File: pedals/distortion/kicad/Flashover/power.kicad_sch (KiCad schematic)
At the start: 13 parts, among them J3 9V DC, U2 TL072, U3 78L05

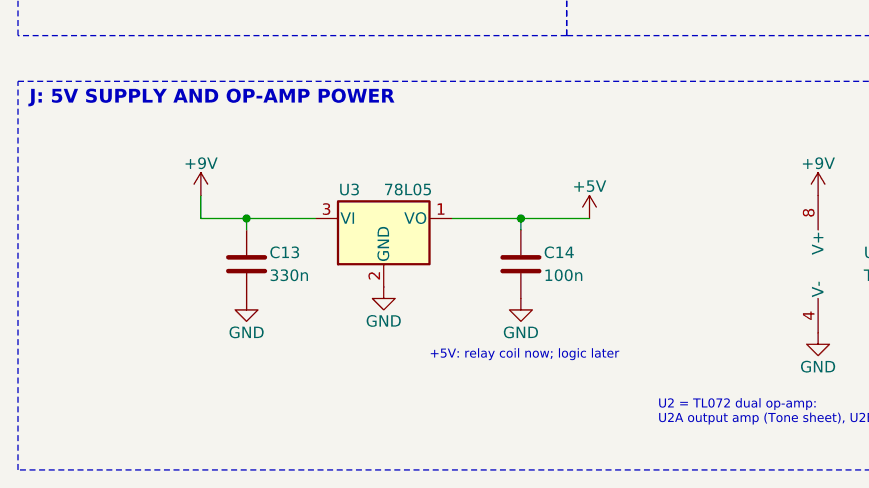
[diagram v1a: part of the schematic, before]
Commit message: Add Flashover controls and LED ring sheets
Controls sheet: three PEC11R encoders with push switches (pull-ups and
RC filtering) and the Soft/Hard button. LED Rings sheet: IS31FL3236A
driving three 11-LED rings plus Soft, Hard and On LEDs, on its own I2C
bus. Controller sheet wires the new GPIOs; the 5V regulator becomes an
L7805 for the LED load. ERC clean.

Co-Authored-By: Claude Opus 5.5 <noreply@anthropic.com>
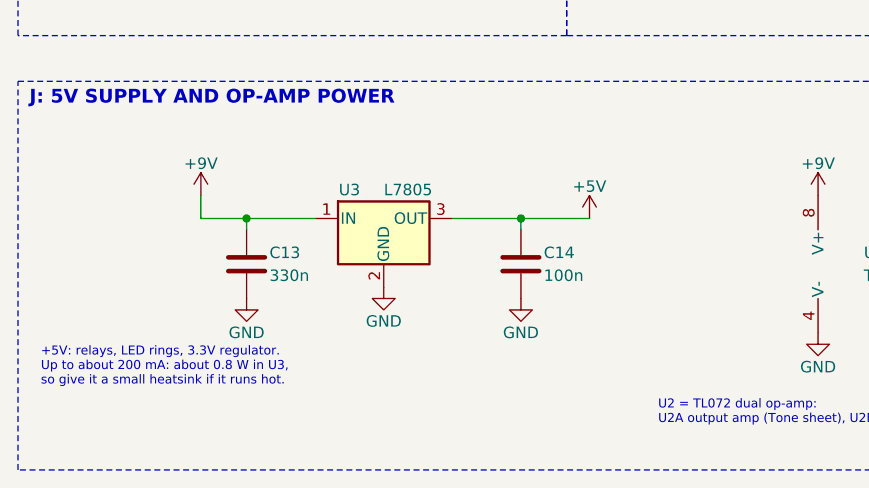
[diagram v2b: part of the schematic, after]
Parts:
- removed U3: 78L05, symbol Regulator_Linear:L78L05_TO92
- added U3: L7805, symbol Regulator_Linear:L7805
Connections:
- net +5V: now also U3.3 (OUT)
- net +9V: now also U3.1 (IN)
- net GND: now also U3.2 (GND)
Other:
- note added: "+5V: relays, LED rings, 3.3V regulator. Up to about 200 mA: about 0.8 W in U3, so give it a small heatsink if it runs hot."
- note removed: "+5V: relay coil now; logic later"
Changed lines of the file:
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@@
 	(title_block
 		(title "Flashover - Power and Bias")
-		(date "2026-10-08")
+		(date "2026-10-09")
 		(rev "0.1")
 		(company "GreywireStudio")
@@
 		(effects (font (size 1 1)) (justify left))
 	)
-	(text "+5V: relay coil now; logic later"
-		(exclude_from_sim no)
-		(at 66.04 139.7 0)
+	(text "+5V: relays, LED rings, 3.3V regulator.\nUp to about 200 mA: about 0.8 W in U3,\nso give it a small heatsink if it runs hot."
+		(exclude_from_sim no)
+		(at 22.86 140.97 0)
 		(effects (font (size 1 1)) (justify left))
 	)
@@
 		(instances
 			(project "Flashover"
-				(path "/37bda491-c0dc-4d48-acdf-49df4f139bb0/553416c4-a47b-4eba-a37d-be64f47f9e32"
+				(path "/ea9f0b88-0903-4174-9c8e-623c203001c6/73170522-0a6a-467c-b01f-a30637312dcb"
 					(reference "J3")
 					(unit 1)
@@
 		(instances
 			(project "Flashover"
-				(path "/37bda491-c0dc-4d48-acdf-49df4f139bb0/553416c4-a47b-4eba-a37d-be64f47f9e32"
+				(path "/ea9f0b88-0903-4174-9c8e-623c203001c6/73170522-0a6a-467c-b01f-a30637312dcb"
 					(reference "D3")
 					(unit 1)
@@
 		(instances
 			(project "Flashover"
-				(path "/37bda491-c0dc-4d48-acdf-49df4f139bb0/553416c4-a47b-4eba-a37d-be64f47f9e32"
+				(path "/ea9f0b88-0903-4174-9c8e-623c203001c6/73170522-0a6a-467c-b01f-a30637312dcb"
 					(reference "#PWR23")
 					(unit 1)
@@
 		(instances
 			(project "Flashover"
-				(path "/37bda491-c0dc-4d48-acdf-49df4f139bb0/553416c4-a47b-4eba-a37d-be64f47f9e32"
+				(path "/ea9f0b88-0903-4174-9c8e-623c203001c6/73170522-0a6a-467c-b01f-a30637312dcb"
 					(reference "#FLG01")
 					(unit 1)
@@
 		(instances
 			(project "Flashover"
-				(path "/37bda491-c0dc-4d48-acdf-49df4f139bb0/553416c4-a47b-4eba-a37d-be64f47f9e32"
+				(path "/ea9f0b88-0903-4174-9c8e-623c203001c6/73170522-0a6a-467c-b01f-a30637312dcb"
 					(reference "#PWR24")
 					(unit 1)
@@
 		(instances
 			(project "Flashover"
-				(path "/37bda491-c0dc-4d48-acdf-49df4f139bb0/553416c4-a47b-4eba-a37d-be64f47f9e32"
+				(path "/ea9f0b88-0903-4174-9c8e-623c203001c6/73170522-0a6a-467c-b01f-a30637312dcb"
 					(reference "C7")
 					(unit 1)
@@
 		(instances
 			(project "Flashover"
-				(path "/37bda491-c0dc-4d48-acdf-49df4f139bb0/553416c4-a47b-4eba-a37d-be64f47f9e32"
+				(path "/ea9f0b88-0903-4174-9c8e-623c203001c6/73170522-0a6a-467c-b01f-a30637312dcb"
 					(reference "#PWR25")
 					(unit 1)
@@
 		(instances
 			(project "Flashover"
-				(path "/37bda491-c0dc-4d48-acdf-49df4f139bb0/553416c4-a47b-4eba-a37d-be64f47f9e32"
+				(path "/ea9f0b88-0903-4174-9c8e-623c203001c6/73170522-0a6a-467c-b01f-a30637312dcb"
 					(reference "#FLG02")
 					(unit 1)
@@
 		(instances
 			(project "Flashover"
-				(path "/37bda491-c0dc-4d48-acdf-49df4f139bb0/553416c4-a47b-4eba-a37d-be64f47f9e32"
+				(path "/ea9f0b88-0903-4174-9c8e-623c203001c6/73170522-0a6a-467c-b01f-a30637312dcb"
 					(reference "#PWR26")
 					(unit 1)
@@
 		(instances
 			(project "Flashover"
-				(path "/37bda491-c0dc-4d48-acdf-49df4f139bb0/553416c4-a47b-4eba-a37d-be64f47f9e32"
+				(path "/ea9f0b88-0903-4174-9c8e-623c203001c6/73170522-0a6a-467c-b01f-a30637312dcb"
 					(reference "R7")
 					(unit 1)
@@
 		(instances
 			(project "Flashover"
-				(path "/37bda491-c0dc-4d48-acdf-49df4f139bb0/553416c4-a47b-4eba-a37d-be64f47f9e32"
+				(path "/ea9f0b88-0903-4174-9c8e-623c203001c6/73170522-0a6a-467c-b01f-a30637312dcb"
 					(reference "R8")
 					(unit 1)
@@
 		(instances
 			(project "Flashover"
-				(path "/37bda491-c0dc-4d48-acdf-49df4f139bb0/553416c4-a47b-4eba-a37d-be64f47f9e32"
+				(path "/ea9f0b88-0903-4174-9c8e-623c203001c6/73170522-0a6a-467c-b01f-a30637312dcb"
 					(reference "#PWR27")
 					(unit 1)
@@
 		(instances
 			(project "Flashover"
-				(path "/37bda491-c0dc-4d48-acdf-49df4f139bb0/553416c4-a47b-4eba-a37d-be64f47f9e32"
+				(path "/ea9f0b88-0903-4174-9c8e-623c203001c6/73170522-0a6a-467c-b01f-a30637312dcb"
 					(reference "C6")
 					(unit 1)
@@
 		(instances
 			(project "Flashover"
-				(path "/37bda491-c0dc-4d48-acdf-49df4f139bb0/553416c4-a47b-4eba-a37d-be64f47f9e32"
+				(path "/ea9f0b88-0903-4174-9c8e-623c203001c6/73170522-0a6a-467c-b01f-a30637312dcb"
 					(reference "#PWR28")
 					(unit 1)
@@
 		(instances
 			(project "Flashover"
-				(path "/37bda491-c0dc-4d48-acdf-49df4f139bb0/553416c4-a47b-4eba-a37d-be64f47f9e32"
+				(path "/ea9f0b88-0903-4174-9c8e-623c203001c6/73170522-0a6a-467c-b01f-a30637312dcb"
 					(reference "U2")
 					(unit 2)
@@
 		(instances
 			(project "Flashover"
-				(path "/37bda491-c0dc-4d48-acdf-49df4f139bb0/553416c4-a47b-4eba-a37d-be64f47f9e32"
+				(path "/ea9f0b88-0903-4174-9c8e-623c203001c6/73170522-0a6a-467c-b01f-a30637312dcb"
 					(reference "R18")
 					(unit 1)
@@
 		(instances
 			(project "Flashover"
-				(path "/37bda491-c0dc-4d48-acdf-49df4f139bb0/553416c4-a47b-4eba-a37d-be64f47f9e32"
+				(path "/ea9f0b88-0903-4174-9c8e-623c203001c6/73170522-0a6a-467c-b01f-a30637312dcb"
 					(reference "C15")
 					(unit 1)
@@
 		(instances
 			(project "Flashover"
-				(path "/37bda491-c0dc-4d48-acdf-49df4f139bb0/553416c4-a47b-4eba-a37d-be64f47f9e32"
+				(path "/ea9f0b88-0903-4174-9c8e-623c203001c6/73170522-0a6a-467c-b01f-a30637312dcb"
 					(reference "#PWR29")
 					(unit 1)
@@
 		(instances
 			(project "Flashover"
-				(path "/37bda491-c0dc-4d48-acdf-49df4f139bb0/553416c4-a47b-4eba-a37d-be64f47f9e32"
+				(path "/ea9f0b88-0903-4174-9c8e-623c203001c6/73170522-0a6a-467c-b01f-a30637312dcb"
 					(reference "#FLG03")
 					(unit 1)
@@
 		(instances
 			(project "Flashover"
-				(path "/37bda491-c0dc-4d48-acdf-49df4f139bb0/553416c4-a47b-4eba-a37d-be64f47f9e32"
+				(path "/ea9f0b88-0903-4174-9c8e-623c203001c6/73170522-0a6a-467c-b01f-a30637312dcb"
 					(reference "#PWR30")
 					(unit 1)
@@
 		(instances
 			(project "Flashover"
-				(path "/37bda491-c0dc-4d48-acdf-49df4f139bb0/553416c4-a47b-4eba-a37d-be64f47f9e32"
+				(path "/ea9f0b88-0903-4174-9c8e-623c203001c6/73170522-0a6a-467c-b01f-a30637312dcb"
 					(reference "#PWR31")
 					(unit 1)
@@
 	)
 	(symbol
-		(lib_id "Regulator_Linear:L78L05_TO92")
+		(lib_id "Regulator_Linear:L7805")
 		(at 60.96 124.46 0)
 		(unit 1)
@@
 			(effects (font (size 1.27 1.27)))
 		)
-		(property "Value" "78L05"
+		(property "Value" "L7805"
 			(at 60.96 121.285 0)
 			(show_name no)
@@
 		(instances
 			(project "Flashover"
-				(path "/37bda491-c0dc-4d48-acdf-49df4f139bb0/553416c4-a47b-4eba-a37d-be64f47f9e32"
+				(path "/ea9f0b88-0903-4174-9c8e-623c203001c6/73170522-0a6a-467c-b01f-a30637312dcb"
 					(reference "U3")
 					(unit 1)
@@
 		(instances
 			(project "Flashover"
-				(path "/37bda491-c0dc-4d48-acdf-49df4f139bb0/553416c4-a47b-4eba-a37d-be64f47f9e32"
+				(path "/ea9f0b88-0903-4174-9c8e-623c203001c6/73170522-0a6a-467c-b01f-a30637312dcb"
 					(reference "C13")
 					(unit 1)
@@
 		(instances
 			(project "Flashover"
-				(path "/37bda491-c0dc-4d48-acdf-49df4f139bb0/553416c4-a47b-4eba-a37d-be64f47f9e32"
+				(path "/ea9f0b88-0903-4174-9c8e-623c203001c6/73170522-0a6a-467c-b01f-a30637312dcb"
 					(reference "#PWR32")
 					(unit 1)
@@
 		(instances
 			(project "Flashover"
-				(path "/37bda491-c0dc-4d48-acdf-49df4f139bb0/553416c4-a47b-4eba-a37d-be64f47f9e32"
+				(path "/ea9f0b88-0903-4174-9c8e-623c203001c6/73170522-0a6a-467c-b01f-a30637312dcb"
 					(reference "#PWR33")
 					(unit 1)
@@
 		(instances
 			(project "Flashover"
-				(path "/37bda491-c0dc-4d48-acdf-49df4f139bb0/553416c4-a47b-4eba-a37d-be64f47f9e32"
+				(path "/ea9f0b88-0903-4174-9c8e-623c203001c6/73170522-0a6a-467c-b01f-a30637312dcb"
 					(reference "C14")
 					(unit 1)
@@
 		(instances
 			(project "Flashover"
-				(path "/37bda491-c0dc-4d48-acdf-49df4f139bb0/553416c4-a47b-4eba-a37d-be64f47f9e32"
+				(path "/ea9f0b88-0903-4174-9c8e-623c203001c6/73170522-0a6a-467c-b01f-a30637312dcb"
 					(reference "#PWR34")
 					(unit 1)
@@
 		(instances
 			(project "Flashover"
-				(path "/37bda491-c0dc-4d48-acdf-49df4f139bb0/553416c4-a47b-4eba-a37d-be64f47f9e32"
+				(path "/ea9f0b88-0903-4174-9c8e-623c203001c6/73170522-0a6a-467c-b01f-a30637312dcb"
 					(reference "#PWR35")
 					(unit 1)
@@
 		(instances
 			(project "Flashover"
-				(path "/37bda491-c0dc-4d48-acdf-49df4f139bb0/553416c4-a47b-4eba-a37d-be64f47f9e32"
+				(path "/ea9f0b88-0903-4174-9c8e-623c203001c6/73170522-0a6a-467c-b01f-a30637312dcb"
 					(reference "U2")
 					(unit 3)
@@
 		(instances
 			(project "Flashover"
-				(path "/37bda491-c0dc-4d48-acdf-49df4f139bb0/553416c4-a47b-4eba-a37d-be64f47f9e32"
+				(path "/ea9f0b88-0903-4174-9c8e-623c203001c6/73170522-0a6a-467c-b01f-a30637312dcb"
 					(reference "#PWR36")
 					(unit 1)
@@
 		(instances
 			(project "Flashover"
-				(path "/37bda491-c0dc-4d48-acdf-49df4f139bb0/553416c4-a47b-4eba-a37d-be64f47f9e32"
+				(path "/ea9f0b88-0903-4174-9c8e-623c203001c6/73170522-0a6a-467c-b01f-a30637312dcb"
 					(reference "#PWR37")
 					(unit 1)
@@
 		(instances
 			(project "Flashover"
-				(path "/37bda491-c0dc-4d48-acdf-49df4f139bb0/553416c4-a47b-4eba-a37d-be64f47f9e32"
+				(path "/ea9f0b88-0903-4174-9c8e-623c203001c6/73170522-0a6a-467c-b01f-a30637312dcb"
 					(reference "C11")
 					(unit 1)
@@
 		(instances
 			(project "Flashover"
-				(path "/37bda491-c0dc-4d48-acdf-49df4f139bb0/553416c4-a47b-4eba-a37d-be64f47f9e32"
+				(path "/ea9f0b88-0903-4174-9c8e-623c203001c6/73170522-0a6a-467c-b01f-a30637312dcb"
 					(reference "#PWR38")
 					(unit 1)
@@
 		(instances
 			(project "Flashover"
-				(path "/37bda491-c0dc-4d48-acdf-49df4f139bb0/553416c4-a47b-4eba-a37d-be64f47f9e32"
+				(path "/ea9f0b88-0903-4174-9c8e-623c203001c6/73170522-0a6a-467c-b01f-a30637312dcb"
 					(reference "#PWR39")
 					(unit 1)

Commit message: Assign Flashover footprints
Surface-mount for assembly; through-hole for jacks, encoders, panel LEDs,
the Soft/Hard button, the TO-220 regulator and the germanium diodes.
Q1/Q2 use the MMBT3904 symbol, 1N4148 -> 1N4148W, 1N5817 -> SS14.

Co-Authored-By: Claude Opus 5.5 <noreply@anthropic.com>
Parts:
- C11, C13, C14: footprint (none) -> Capacitor_SMD:C_0805_2012Metric
- C15, C6: footprint (none) -> Capacitor_SMD:CP_Elec_5x5.4
- C7: footprint (none) -> Capacitor_SMD:CP_Elec_6.3x5.4
- D3: value 1N5817 -> SS14; footprint (none) -> Diode_SMD:D_SMA
- J3: footprint (none) -> Connector_BarrelJack:BarrelJack_CUI_PJ-102AH_Horizontal
- R18, R7, R8: footprint (none) -> Resistor_SMD:R_0805_2012Metric
- U2: footprint (none) -> Package_SO:SOIC-8_3.9x4.9mm_P1.27mm
- U3: footprint (none) -> Package_TO_SOT_THT:TO-220-3_Vertical

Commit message: Split Flashover into main and control boards; place parts
Main board (Flashover): audio, controller, pots, MIDI, bypass and the five
top-mounted jacks.  Control board (Flashover_Controls): encoders, LED rings,
LED driver, Soft/Hard button and panel LEDs.  J7/J8 2x10 board connector,
M3 mounting holes, regulator laid flat.  Placement only, not yet routed.

Co-Authored-By: Claude Opus 5.5 <noreply@anthropic.com>
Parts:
- U3: footprint Package_TO_SOT_THT:TO-220-3_Vertical -> Package_TO_SOT_THT:TO-220-3_Horizontal_TabDown
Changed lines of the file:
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@@
 		(instances
 			(project "Flashover"
-				(path "/872055d3-e01a-4a82-8c05-28c93674a700/c3224ece-4901-49d6-b919-c4688692a053"
+				(path "/837bea85-92fd-51b5-9680-1e9b1b02f616/2576b1fc-88e7-5e62-97c6-8c7b62c813c9"
 					(reference "J3")
 					(unit 1)
@@
 		(instances
 			(project "Flashover"
-				(path "/872055d3-e01a-4a82-8c05-28c93674a700/c3224ece-4901-49d6-b919-c4688692a053"
+				(path "/837bea85-92fd-51b5-9680-1e9b1b02f616/2576b1fc-88e7-5e62-97c6-8c7b62c813c9"
 					(reference "D3")
 					(unit 1)
@@
 		(instances
 			(project "Flashover"
-				(path "/872055d3-e01a-4a82-8c05-28c93674a700/c3224ece-4901-49d6-b919-c4688692a053"
+				(path "/837bea85-92fd-51b5-9680-1e9b1b02f616/2576b1fc-88e7-5e62-97c6-8c7b62c813c9"
 					(reference "#PWR21")
 					(unit 1)
@@
 		(instances
 			(project "Flashover"
-				(path "/872055d3-e01a-4a82-8c05-28c93674a700/c3224ece-4901-49d6-b919-c4688692a053"
+				(path "/837bea85-92fd-51b5-9680-1e9b1b02f616/2576b1fc-88e7-5e62-97c6-8c7b62c813c9"
 					(reference "#FLG01")
 					(unit 1)
@@
 		(instances
 			(project "Flashover"
-				(path "/872055d3-e01a-4a82-8c05-28c93674a700/c3224ece-4901-49d6-b919-c4688692a053"
+				(path "/837bea85-92fd-51b5-9680-1e9b1b02f616/2576b1fc-88e7-5e62-97c6-8c7b62c813c9"
 					(reference "#PWR22")
 					(unit 1)
@@
 		(instances
 			(project "Flashover"
-				(path "/872055d3-e01a-4a82-8c05-28c93674a700/c3224ece-4901-49d6-b919-c4688692a053"
+				(path "/837bea85-92fd-51b5-9680-1e9b1b02f616/2576b1fc-88e7-5e62-97c6-8c7b62c813c9"
 					(reference "C7")
 					(unit 1)
@@
 		(instances
 			(project "Flashover"
-				(path "/872055d3-e01a-4a82-8c05-28c93674a700/c3224ece-4901-49d6-b919-c4688692a053"
+				(path "/837bea85-92fd-51b5-9680-1e9b1b02f616/2576b1fc-88e7-5e62-97c6-8c7b62c813c9"
 					(reference "#PWR23")
 					(unit 1)
@@
 		(instances
 			(project "Flashover"
-				(path "/872055d3-e01a-4a82-8c05-28c93674a700/c3224ece-4901-49d6-b919-c4688692a053"
+				(path "/837bea85-92fd-51b5-9680-1e9b1b02f616/2576b1fc-88e7-5e62-97c6-8c7b62c813c9"
 					(reference "#FLG02")
 					(unit 1)
@@
 		(instances
 			(project "Flashover"
-				(path "/872055d3-e01a-4a82-8c05-28c93674a700/c3224ece-4901-49d6-b919-c4688692a053"
+				(path "/837bea85-92fd-51b5-9680-1e9b1b02f616/2576b1fc-88e7-5e62-97c6-8c7b62c813c9"
 					(reference "#PWR24")
 					(unit 1)
@@
 		(instances
 			(project "Flashover"
-				(path "/872055d3-e01a-4a82-8c05-28c93674a700/c3224ece-4901-49d6-b919-c4688692a053"
+				(path "/837bea85-92fd-51b5-9680-1e9b1b02f616/2576b1fc-88e7-5e62-97c6-8c7b62c813c9"
 					(reference "R7")
 					(unit 1)
@@
 		(instances
 			(project "Flashover"
-				(path "/872055d3-e01a-4a82-8c05-28c93674a700/c3224ece-4901-49d6-b919-c4688692a053"
+				(path "/837bea85-92fd-51b5-9680-1e9b1b02f616/2576b1fc-88e7-5e62-97c6-8c7b62c813c9"
 					(reference "R8")
 					(unit 1)
@@
 		(instances
 			(project "Flashover"
-				(path "/872055d3-e01a-4a82-8c05-28c93674a700/c3224ece-4901-49d6-b919-c4688692a053"
+				(path "/837bea85-92fd-51b5-9680-1e9b1b02f616/2576b1fc-88e7-5e62-97c6-8c7b62c813c9"
 					(reference "#PWR25")
 					(unit 1)
@@
 		(instances
 			(project "Flashover"
-				(path "/872055d3-e01a-4a82-8c05-28c93674a700/c3224ece-4901-49d6-b919-c4688692a053"
+				(path "/837bea85-92fd-51b5-9680-1e9b1b02f616/2576b1fc-88e7-5e62-97c6-8c7b62c813c9"
 					(reference "C6")
 					(unit 1)
@@
 		(instances
 			(project "Flashover"
-				(path "/872055d3-e01a-4a82-8c05-28c93674a700/c3224ece-4901-49d6-b919-c4688692a053"
+				(path "/837bea85-92fd-51b5-9680-1e9b1b02f616/2576b1fc-88e7-5e62-97c6-8c7b62c813c9"
 					(reference "#PWR26")
 					(unit 1)
@@
 		(instances
 			(project "Flashover"
-				(path "/872055d3-e01a-4a82-8c05-28c93674a700/c3224ece-4901-49d6-b919-c4688692a053"
+				(path "/837bea85-92fd-51b5-9680-1e9b1b02f616/2576b1fc-88e7-5e62-97c6-8c7b62c813c9"
 					(reference "U2")
 					(unit 2)
@@
 		(instances
 			(project "Flashover"
-				(path "/872055d3-e01a-4a82-8c05-28c93674a700/c3224ece-4901-49d6-b919-c4688692a053"
+				(path "/837bea85-92fd-51b5-9680-1e9b1b02f616/2576b1fc-88e7-5e62-97c6-8c7b62c813c9"
 					(reference "R18")
 					(unit 1)
@@
 		(instances
 			(project "Flashover"
-				(path "/872055d3-e01a-4a82-8c05-28c93674a700/c3224ece-4901-49d6-b919-c4688692a053"
+				(path "/837bea85-92fd-51b5-9680-1e9b1b02f616/2576b1fc-88e7-5e62-97c6-8c7b62c813c9"
 					(reference "C15")
 					(unit 1)
@@
 		(instances
 			(project "Flashover"
-				(path "/872055d3-e01a-4a82-8c05-28c93674a700/c3224ece-4901-49d6-b919-c4688692a053"
+				(path "/837bea85-92fd-51b5-9680-1e9b1b02f616/2576b1fc-88e7-5e62-97c6-8c7b62c813c9"
 					(reference "#PWR27")
 					(unit 1)
@@
 		(instances
 			(project "Flashover"
-				(path "/872055d3-e01a-4a82-8c05-28c93674a700/c3224ece-4901-49d6-b919-c4688692a053"
+				(path "/837bea85-92fd-51b5-9680-1e9b1b02f616/2576b1fc-88e7-5e62-97c6-8c7b62c813c9"
 					(reference "#FLG03")
 					(unit 1)
@@
 		(instances
 			(project "Flashover"
-				(path "/872055d3-e01a-4a82-8c05-28c93674a700/c3224ece-4901-49d6-b919-c4688692a053"
+				(path "/837bea85-92fd-51b5-9680-1e9b1b02f616/2576b1fc-88e7-5e62-97c6-8c7b62c813c9"
 					(reference "#PWR28")
 					(unit 1)
@@
 		(instances
 			(project "Flashover"
-				(path "/872055d3-e01a-4a82-8c05-28c93674a700/c3224ece-4901-49d6-b919-c4688692a053"
+				(path "/837bea85-92fd-51b5-9680-1e9b1b02f616/2576b1fc-88e7-5e62-97c6-8c7b62c813c9"
 					(reference "#PWR29")
 					(unit 1)
@@
 			(effects (font (size 1.27 1.27)) (justify left))
 		)
-		(property "Footprint" "Package_TO_SOT_THT:TO-220-3_Vertical"
+		(property "Footprint" "Package_TO_SOT_THT:TO-220-3_Horizontal_TabDown"
 			(at 60.96 124.46 0)
 			(hide yes)
@@
 		(instances
 			(project "Flashover"
-				(path "/872055d3-e01a-4a82-8c05-28c93674a700/c3224ece-4901-49d6-b919-c4688692a053"
+				(path "/837bea85-92fd-51b5-9680-1e9b1b02f616/2576b1fc-88e7-5e62-97c6-8c7b62c813c9"
 					(reference "U3")
 					(unit 1)
@@
 		(instances
 			(project "Flashover"
-				(path "/872055d3-e01a-4a82-8c05-28c93674a700/c3224ece-4901-49d6-b919-c4688692a053"
+				(path "/837bea85-92fd-51b5-9680-1e9b1b02f616/2576b1fc-88e7-5e62-97c6-8c7b62c813c9"
 					(reference "C13")
 					(unit 1)
@@
 		(instances
 			(project "Flashover"
-				(path "/872055d3-e01a-4a82-8c05-28c93674a700/c3224ece-4901-49d6-b919-c4688692a053"
+				(path "/837bea85-92fd-51b5-9680-1e9b1b02f616/2576b1fc-88e7-5e62-97c6-8c7b62c813c9"
 					(reference "#PWR30")
 					(unit 1)
@@
 		(instances
 			(project "Flashover"
-				(path "/872055d3-e01a-4a82-8c05-28c93674a700/c3224ece-4901-49d6-b919-c4688692a053"
+				(path "/837bea85-92fd-51b5-9680-1e9b1b02f616/2576b1fc-88e7-5e62-97c6-8c7b62c813c9"
 					(reference "#PWR31")
 					(unit 1)
@@
 		(instances
 			(project "Flashover"
-				(path "/872055d3-e01a-4a82-8c05-28c93674a700/c3224ece-4901-49d6-b919-c4688692a053"
+				(path "/837bea85-92fd-51b5-9680-1e9b1b02f616/2576b1fc-88e7-5e62-97c6-8c7b62c813c9"
 					(reference "C14")
 					(unit 1)
@@
 		(instances
 			(project "Flashover"
-				(path "/872055d3-e01a-4a82-8c05-28c93674a700/c3224ece-4901-49d6-b919-c4688692a053"
+				(path "/837bea85-92fd-51b5-9680-1e9b1b02f616/2576b1fc-88e7-5e62-97c6-8c7b62c813c9"
 					(reference "#PWR32")
 					(unit 1)
@@
 		(instances
 			(project "Flashover"
-				(path "/872055d3-e01a-4a82-8c05-28c93674a700/c3224ece-4901-49d6-b919-c4688692a053"
+				(path "/837bea85-92fd-51b5-9680-1e9b1b02f616/2576b1fc-88e7-5e62-97c6-8c7b62c813c9"
 					(reference "#PWR33")
 					(unit 1)
@@
 		(instances
 			(project "Flashover"
-				(path "/872055d3-e01a-4a82-8c05-28c93674a700/c3224ece-4901-49d6-b919-c4688692a053"
+				(path "/837bea85-92fd-51b5-9680-1e9b1b02f616/2576b1fc-88e7-5e62-97c6-8c7b62c813c9"
 					(reference "U2")
 					(unit 3)
@@
 		(instances
 			(project "Flashover"
-				(path "/872055d3-e01a-4a82-8c05-28c93674a700/c3224ece-4901-49d6-b919-c4688692a053"
+				(path "/837bea85-92fd-51b5-9680-1e9b1b02f616/2576b1fc-88e7-5e62-97c6-8c7b62c813c9"
 					(reference "#PWR34")
 					(unit 1)
@@
 		(instances
 			(project "Flashover"
-				(path "/872055d3-e01a-4a82-8c05-28c93674a700/c3224ece-4901-49d6-b919-c4688692a053"
+				(path "/837bea85-92fd-51b5-9680-1e9b1b02f616/2576b1fc-88e7-5e62-97c6-8c7b62c813c9"
 					(reference "#PWR35")
 					(unit 1)
@@
 		(instances
 			(project "Flashover"
-				(path "/872055d3-e01a-4a82-8c05-28c93674a700/c3224ece-4901-49d6-b919-c4688692a053"
+				(path "/837bea85-92fd-51b5-9680-1e9b1b02f616/2576b1fc-88e7-5e62-97c6-8c7b62c813c9"
 					(reference "C11")
 					(unit 1)
@@
 		(instances
 			(project "Flashover"
-				(path "/872055d3-e01a-4a82-8c05-28c93674a700/c3224ece-4901-49d6-b919-c4688692a053"
+				(path "/837bea85-92fd-51b5-9680-1e9b1b02f616/2576b1fc-88e7-5e62-97c6-8c7b62c813c9"
 					(reference "#PWR36")
 					(unit 1)
@@
 		(instances
 			(project "Flashover"
-				(path "/872055d3-e01a-4a82-8c05-28c93674a700/c3224ece-4901-49d6-b919-c4688692a053"
+				(path "/837bea85-92fd-51b5-9680-1e9b1b02f616/2576b1fc-88e7-5e62-97c6-8c7b62c813c9"
 					(reference "#PWR37")
 					(unit 1)
